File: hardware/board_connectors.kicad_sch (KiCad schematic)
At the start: 15 parts, among them J1 AudioJack2_Ground, J3 Conn_01x02, J5 AudioJack2_Ground, J6 Conn_02x03_Odd_Even, J7 AudioJack2_Ground, J7 USB_B_Micro

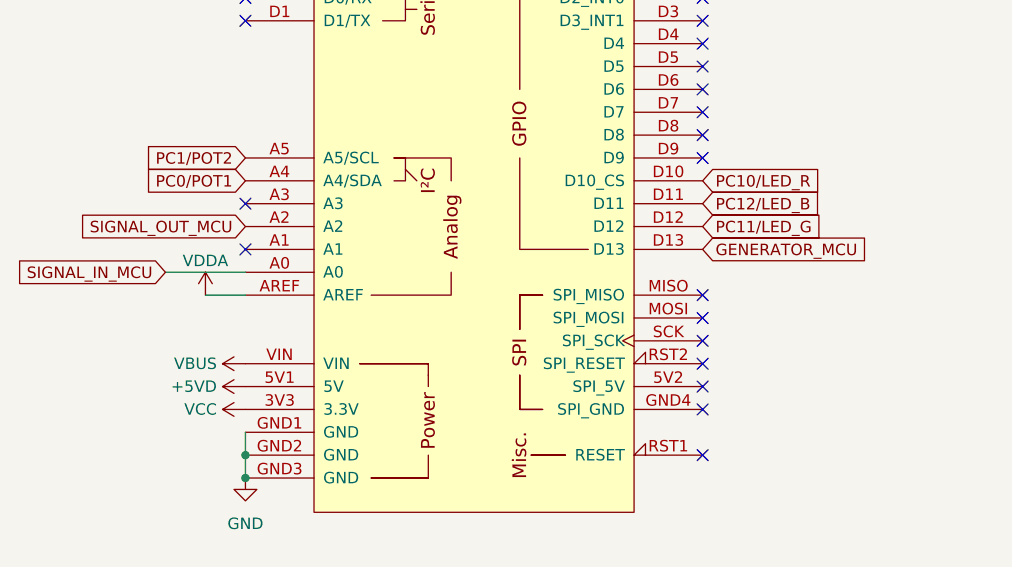
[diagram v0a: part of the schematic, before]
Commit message: wip: schematic fixes based on testing
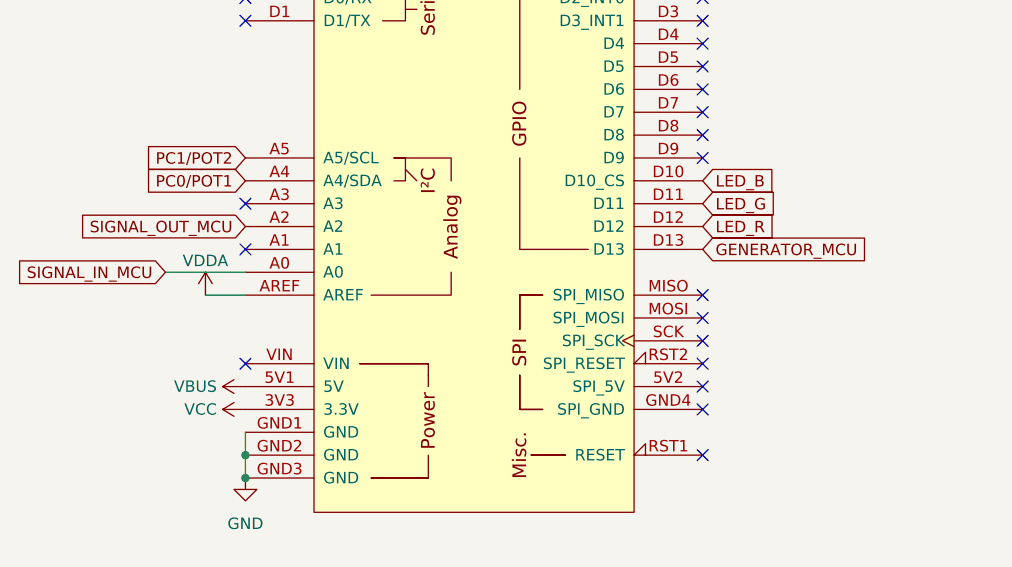
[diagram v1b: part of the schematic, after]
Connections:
- net +5VD is gone; now on net VBUS: A2.5V1 (5V)
- net VBUS: no longer A2.VIN
- net PC10/LED_R renamed LED_B
- net PC11/LED_G renamed LED_R
- net PC12/LED_B renamed LED_G
- no-connect marks 20 -> 21
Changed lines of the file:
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@@
   (title_block
     (title "DSP PAW add-on board")
-    (date "2023-08-19")
+    (date "2023-09-04")
+    (rev "2")
     (company "bitgloo")
     (comment 1 "Released under the CERN Open Hardware Licence Version 2 - Strongly Reciprocal")
@@
   (no_connect (at 100.33 46.99))
   (no_connect (at 100.33 80.01))
+  (no_connect (at 49.53 87.63))
   (no_connect (at 100.33 52.07))
   (no_connect (at 100.33 87.63))
@@
     )
   )
-  (global_label "PC10{slash}LED_R" (shape input) (at 100.33 67.31 0) (fields_autoplaced)
+  (global_label "LED_B" (shape input) (at 100.33 67.31 0) (fields_autoplaced)
     (effects (font (size 1.27 1.27)) (justify left))
-    (property "Intersheetrefs" "${INTERSHEET_REFS}" (at 115.21 67.31 0)
+    (property "Intersheetrefs" "${INTERSHEET_REFS}" (at 108.9205 67.31 0)
       (effects (font (size 1.27 1.27)) (justify left) hide)
     )
@@
     )
   )
-  (global_label "PC12{slash}LED_B" (shape input) (at 100.33 69.85 0) (fields_autoplaced)
+  (global_label "LED_G" (shape input) (at 100.33 69.85 0) (fields_autoplaced)
     (effects (font (size 1.27 1.27)) (justify left))
-    (property "Intersheetrefs" "${INTERSHEET_REFS}" (at 115.21 69.85 0)
+    (property "Intersheetrefs" "${INTERSHEET_REFS}" (at 108.9205 69.85 0)
       (effects (font (size 1.27 1.27)) (justify left) hide)
     )
   )
-  (global_label "PC11{slash}LED_G" (shape input) (at 100.33 72.39 0) (fields_autoplaced)
+  (global_label "LED_R" (shape input) (at 100.33 72.39 0) (fields_autoplaced)
     (effects (font (size 1.27 1.27)) (justify left))
-    (property "Intersheetrefs" "${INTERSHEET_REFS}" (at 114.7174 72.3106 0)
+    (property "Intersheetrefs" "${INTERSHEET_REFS}" (at 108.9205 72.39 0)
       (effects (font (size 1.27 1.27)) (justify left) hide)
     )
@@
     )
   )
-  (symbol (lib_id "power:VBUS") (at 49.53 87.63 90) (unit 1)
+  (symbol (lib_id "power:VBUS") (at 49.53 90.17 90) (unit 1)
     (in_bom yes) (on_board yes) (dnp no)
-    (property "Reference" "#PWR075" (at 53.34 87.63 0)
-      (effects (font (size 1.27 1.27)) hide)
-    )
-    (property "Value" "VBUS" (at 46.355 87.63 90)
+    (property "Reference" "#PWR075" (at 53.34 90.17 0)
+      (effects (font (size 1.27 1.27)) hide)
+    )
+    (property "Value" "VBUS" (at 46.355 90.17 90)
       (effects (font (size 1.27 1.27)) (justify left))
     )
-    (property "Footprint" "" (at 49.53 87.63 0)
-      (effects (font (size 1.27 1.27)) hide)
-    )
-    (property "Datasheet" "" (at 49.53 87.63 0)
+    (property "Footprint" "" (at 49.53 90.17 0)
+      (effects (font (size 1.27 1.27)) hide)
+    )
+    (property "Datasheet" "" (at 49.53 90.17 0)
       (effects (font (size 1.27 1.27)) hide)
     )
@@
         )
       )
-    )
-  )
-  (symbol (lib_id "power:+5VD") (at 49.53 90.17 90) (unit 1)
-    (in_bom yes) (on_board yes) (dnp no)
-    (property "Reference" "#PWR047" (at 53.34 90.17 0)
-      (effects (font (size 1.27 1.27)) hide)
-    )
-    (property "Value" "+5VD" (at 46.355 90.17 90)
-      (effects (font (size 1.27 1.27)) (justify left))
-    )
-    (property "Footprint" "" (at 49.53 90.17 0)
-      (effects (font (size 1.27 1.27)) hide)
-    )
-    (property "Datasheet" "" (at 49.53 90.17 0)
-      (effects (font (size 1.27 1.27)) hide)
-    )
-    (pin "1")
-    (instances
-      (project "DSP PAW add-on board"
-        (path "/c291319b-d76e-4fda-91cc-061acff65f9f/270d19d2-3af2-41db-ad1c-33373417ec82"
-          (reference "#PWR047") (unit 1)
-        )
-      )

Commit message: vdda buffer; vdda for pots; other fixes
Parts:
- D1, D2, D3: LCSC Part # C475683 -> (none)
- D4, D5, D6: LCSC Part # C1972965 -> (none)
- J1, J5, J7: LCSC Part # C431535 -> (none)
- J6: LCSC Part # C65114 -> (none)
- J7: LCSC Part # C428496 -> (none)
- R22, R6: LCSC Part # C21189 -> (none)
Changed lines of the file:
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@@
-      (effects (font (size 1.27 1.27)) hide)
-    )
-    (property "LCSC Part #" "C1972965" (at 55.88 166.37 0)
       (effects (font (size 1.27 1.27)) hide)
     )
@@
     )
     (property "DNP" "T" (at 74.93 73.66 0)
-      (effects (font (size 1.27 1.27)) hide)
-    )
-    (property "LCSC Part #" "" (at 74.93 73.66 0)
       (effects (font (size 1.27 1.27)) hide)
     )
@@
       (effects (font (size 1.27 1.27)) hide)
     )
-    (property "LCSC Part #" "C1972965" (at 64.77 166.37 0)
-      (effects (font (size 1.27 1.27)) hide)
-    )
     (pin "1")
     (pin "2")
@@
     )
     (property "DNP" "" (at 177.8 85.09 0)
-      (effects (font (size 1.27 1.27)) hide)
-    )
-    (property "LCSC Part #" "C431535" (at 177.8 85.09 0)
       (effects (font (size 1.27 1.27)) hide)
     )
@@
       (effects (font (size 1.27 1.27)) hide)
     )
-    (property "LCSC Part #" "C475683" (at 194.31 123.19 0)
-      (effects (font (size 1.27 1.27)) hide)
-    )
     (pin "1")
     (pin "2")
@@
       (effects (font (size 1.27 1.27)) hide)
     )
-    (property "LCSC Part #" "C475683" (at 194.31 60.96 0)
-      (effects (font (size 1.27 1.27)) hide)
-    )
     (pin "1")
     (pin "2")
@@
       (effects (font (size 1.27 1.27)) hide)
     )
-    (property "LCSC Part #" "C475683" (at 194.31 91.44 0)
-      (effects (font (size 1.27 1.27)) hide)
-    )
     (pin "1")
     (pin "2")
@@
     )
     (property "DNP" "" (at 177.8 54.61 0)
-      (effects (font (size 1.27 1.27)) hide)
-    )
-    (property "LCSC Part #" "C431535" (at 177.8 54.61 0)
       (effects (font (size 1.27 1.27)) hide)
     )
@@
     )
     (property "DNP" "" (at 41.91 153.67 0)
-      (effects (font (size 1.27 1.27)) hide)
-    )
-    (property "LCSC Part #" "C428496" (at 41.91 153.67 0)
       (effects (font (size 1.27 1.27)) hide)
     )
@@
       (effects (font (size 1.27 1.27)) hide)
     )
-    (property "LCSC Part #" "C21189" (at 186.69 123.19 0)
-      (effects (font (size 1.27 1.27)) hide)
-    )
     (pin "1")
     (pin "2")
@@
     )
     (property "DNP" "" (at 177.8 116.84 0)
-      (effects (font (size 1.27 1.27)) hide)
-    )
-    (property "LCSC Part #" "C431535" (at 177.8 116.84 0)
       (effects (font (size 1.27 1.27)) hide)
     )
@@
       (effects (font (size 1.27 1.27)) hide)
     )
-    (property "LCSC Part #" "C21189" (at 39.37 168.91 0)
-      (effects (font (size 1.27 1.27)) hide)
-    )
     (pin "1")
     (pin "2")
@@
     )
     (property "DNP" "T" (at 124.46 153.67 0)
-      (effects (font (size 1.27 1.27)) hide)
-    )
-    (property "LCSC Part #" "" (at 124.46 153.67 0)
       (effects (font (size 1.27 1.27)) hide)
     )
@@
       (effects (font (size 1.27 1.27)) hide)
     )
-    (property "LCSC Part #" "C1972965" (at 73.66 166.37 0)
-      (effects (font (size 1.27 1.27)) hide)
-    )
     (pin "1")
     (pin "2")
@@
       (effects (font (size 1.27 1.27)) hide)
     )
-    (property "LCSC Part #" "C65114" (at 243.84 72.39 0)
-      (effects (font (size 1.27 1.27)) hide)
-    )
